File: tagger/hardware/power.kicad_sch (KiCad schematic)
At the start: 14 parts, among them J6 TETHER_POWER, U15 TPS560200

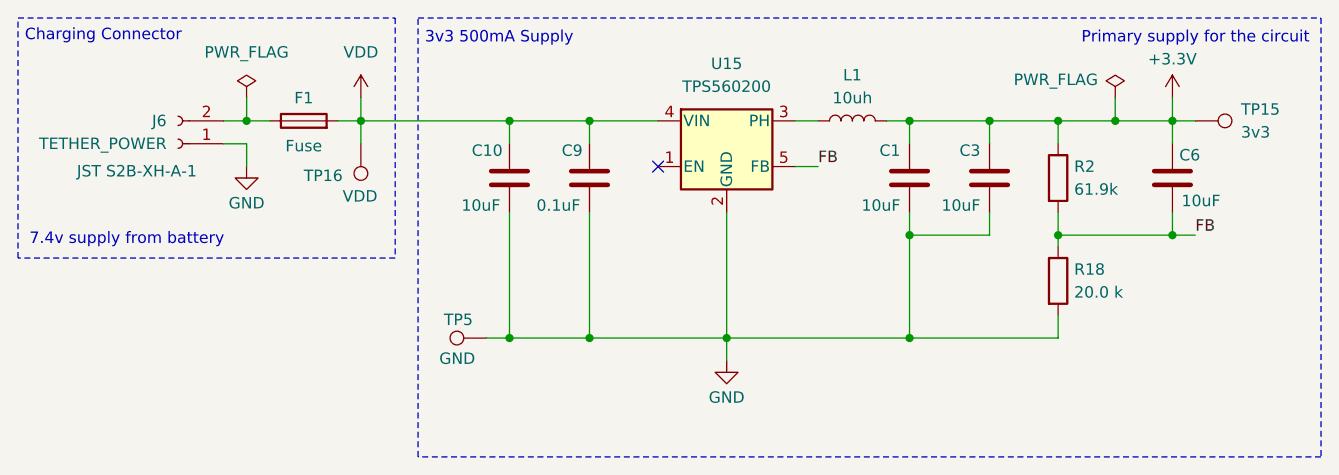
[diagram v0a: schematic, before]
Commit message: feat: schematic organization, added SD card connections
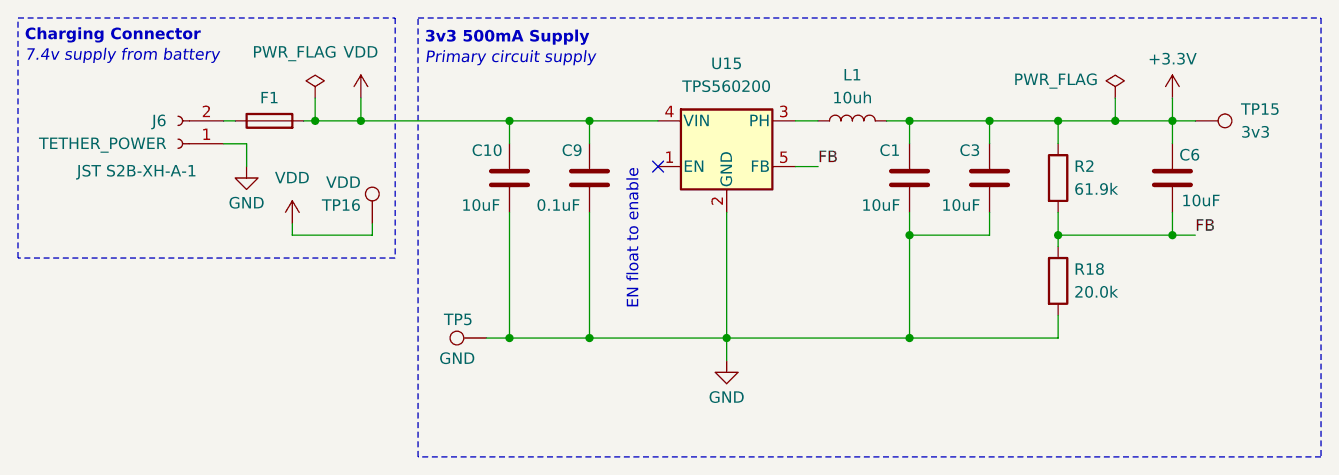
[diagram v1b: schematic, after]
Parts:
- R18: value 20.0 k -> 20.0k
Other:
- note added: "EN float to enable"
- note added: "Primary circuit supply"
- note removed: "Primary supply for the circuit"
- moved on the sheet: F1, TP16
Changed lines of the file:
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@@
 			(font
 				(size 1.27 1.27)
+				(thickness 0.254)
+				(bold yes)
 			)
 			(justify left top)
@@
 	(text "7.4v supply from battery"
 		(exclude_from_sim no)
-		(at 19.05 43.18 0)
+		(at 18.542 21.336 0)
+		(effects
+			(font
+				(size 1.27 1.27)
+				(italic yes)
+				(color 194 194 194 1)
+			)
+			(justify left top)
+		)
+	)
+	(text "Primary circuit supply"
+		(exclude_from_sim no)
+		(at 62.992 21.59 0)
+		(effects
+			(font
+				(size 1.27 1.27)
+				(italic yes)
+				(color 194 194 194 1)
+			)
+			(justify left top)
+		)
+	)
+	(text "EN float to enable"
+		(exclude_from_sim no)
+		(at 86.106 42.418 90)
 		(effects
 			(font
@@
 				(color 132 132 132 1)
 			)
-			(justify left bottom)
-		)
-	)
-	(text "Primary supply for the circuit"
-		(exclude_from_sim no)
-		(at 161.29 19.304 0)
-		(effects
-			(font
-				(size 1.27 1.27)
-				(color 132 132 132 1)
-			)
-			(justify right top)
 		)
 	)
@@
 			(font
 				(size 1.27 1.27)
+				(thickness 0.254)
+				(bold yes)
 			)
 			(justify left top)
@@
 	)
 	(junction
-		(at 133.35 41.91)
+		(at 50.8 29.21)
 		(diameter 0)
 		(color 0 0 0 0)
 	)
 	(junction
-		(at 43.18 29.21)
+		(at 133.35 41.91)
 		(diameter 0)
 		(color 0 0 0 0)
@@
 	(wire
 		(pts
-			(xy 55.88 29.21) (xy 55.88 31.75)
+			(xy 57.15 40.64) (xy 57.15 41.91)
 		)
 		(stroke
@@
 	(wire
 		(pts
-			(xy 53.34 29.21) (xy 55.88 29.21)
-		)
-		(stroke
-			(width 0)
-			(type default)
-		)
-	)
-	(wire
-		(pts
 			(xy 72.39 39.37) (xy 72.39 53.34)
 		)
@@
 	(wire
 		(pts
+			(xy 48.26 41.91) (xy 57.15 41.91)
+		)
+		(stroke
+			(width 0)
+			(type default)
+		)
+	)
+	(wire
+		(pts
 			(xy 133.35 50.8) (xy 133.35 53.34)
 		)
@@
 	(wire
 		(pts
+			(xy 48.26 40.64) (xy 48.26 41.91)
+		)
+		(stroke
+			(width 0)
+			(type default)
+		)
+	)
+	(wire
+		(pts
 			(xy 125.73 29.21) (xy 125.73 31.75)
 		)
@@
 	(wire
 		(pts
-			(xy 43.18 26.67) (xy 43.18 29.21)
+			(xy 50.8 26.67) (xy 50.8 29.21)
 		)
 		(stroke
@@
 	(wire
 		(pts
-			(xy 40.64 29.21) (xy 43.18 29.21)
+			(xy 40.64 29.21) (xy 41.91 29.21)
 		)
 		(stroke
@@
 	(wire
 		(pts
+			(xy 50.8 29.21) (xy 55.88 29.21)
+		)
+		(stroke
+			(width 0)
+			(type default)
+		)
+	)
+	(wire
+		(pts
 			(xy 146.05 29.21) (xy 148.59 29.21)
 		)
@@
 	(wire
 		(pts
-			(xy 43.18 29.21) (xy 45.72 29.21)
-		)
-		(stroke
-			(width 0)
-			(type default)
-		)
-	)
-	(wire
-		(pts
 			(xy 116.84 41.91) (xy 116.84 53.34)
 		)
@@
 		(pts
 			(xy 116.84 29.21) (xy 125.73 29.21)
+		)
+		(stroke
+			(width 0)
+			(type default)
+		)
+	)
+	(wire
+		(pts
+			(xy 49.53 29.21) (xy 50.8 29.21)
 		)
 		(stroke
@@
 	(symbol
 		(lib_id "power:PWR_FLAG")
-		(at 43.18 26.67 0)
+		(at 50.8 26.67 0)
 		(unit 1)
 		(exclude_from_sim no)
@@
 		(on_board yes)
 		(dnp no)
-		(fields_autoplaced yes)
 		(property "Reference" "#FLG01"
-			(at 43.18 24.765 0)
+			(at 50.8 24.765 0)
 			(effects
 				(font
@@
 		)
 		(property "Value" "PWR_FLAG"
-			(at 43.18 21.59 0)
+			(at 48.514 21.59 0)
 			(effects
 				(font
@@
 		)
 		(property "Footprint" ""
-			(at 43.18 26.67 0)
+			(at 50.8 26.67 0)
 			(effects
 				(font
@@
 		)
 		(property "Datasheet" "~"
-			(at 43.18 26.67 0)
+			(at 50.8 26.67 0)
 			(effects
 				(font
@@
 		)
 		(property "Description" "Special symbol for telling ERC where power comes from"
-			(at 43.18 26.67 0)
+			(at 50.8 26.67 0)
 			(effects
 				(font
@@
 	(symbol
 		(lib_id "Connector:TestPoint")
-		(at 55.88 31.75 0)
-		(mirror x)
+		(at 57.15 40.64 0)
 		(unit 1)
 		(exclude_from_sim no)
@@
 		(dnp no)
 		(property "Reference" "TP16"
-			(at 49.53 35.306 0)
-			(effects
-				(font
-					(size 1.27 1.27)
-				)
-				(justify left)
+			(at 55.88 38.608 0)
+			(effects
+				(font
+					(size 1.27 1.27)
+				)
+				(justify right)
 			)
 		)
 		(property "Value" "VDD"
-			(at 53.848 37.592 0)
-			(effects
-				(font
-					(size 1.27 1.27)
-				)
-				(justify left)
+			(at 55.88 36.068 0)
+			(effects
+				(font
+					(size 1.27 1.27)
+				)
+				(justify right)
 			)
 		)
 		(property "Footprint" "TestPoint:TestPoint_Pad_D1.5mm"
-			(at 60.96 31.75 0)
+			(at 62.23 40.64 0)
 			(effects
 				(font
@@
 		)
 		(property "Datasheet" "~"
-			(at 60.96 31.75 0)
+			(at 62.23 40.64 0)
 			(effects
 				(font
@@
 		)
 		(property "Description" "test point"
-			(at 55.88 31.75 0)
+			(at 57.15 40.64 0)
 			(effects
 				(font
@@
 		)
 		(property "Height" ""
-			(at 55.88 31.75 0)
+			(at 57.15 40.64 0)
 			(effects
 				(font
@@
 		)
 		(property "Manufacturer_Name" ""
-			(at 55.88 31.75 0)
+			(at 57.15 40.64 0)
 			(effects
 				(font
@@
 		)
 		(property "Manufacturer_Part_Number" ""
-			(at 55.88 31.75 0)
+			(at 57.15 40.64 0)
 			(effects
 				(font
@@
 		)
 		(property "Mouser Part Number" ""
-			(at 55.88 31.75 0)
+			(at 57.15 40.64 0)
 			(effects
 				(font
@@
 		)
 		(property "Mouser Price/Stock" ""
-			(at 55.88 31.75 0)
+			(at 57.15 40.64 0)
 			(effects
 				(font
@@
 		)
 		(property "JLC" ""
-			(at 55.88 31.75 0)
+			(at 57.15 40.64 0)
 			(effects
 				(font
@@
 	(symbol
 		(lib_id "Device:Fuse")
-		(at 49.53 29.21 90)
+		(at 45.72 29.21 90)
 		(unit 1)
 		(exclude_from_sim no)
@@
 		(dnp no)
 		(property "Reference" "F1"
-			(at 49.53 26.67 90)
+			(at 45.72 26.67 90)
 			(effects
 				(font
@@
 		)
 		(property "Value" "Fuse"
-			(at 49.53 32.004 90)
-			(effects
-				(font
-					(size 1.27 1.27)
-				)
+			(at 45.72 31.496 90)
+			(effects
+				(font
+					(size 1.27 1.27)
+				)
+				(hide yes)
 			)
 		)
 		(property "Footprint" "Fuse:Fuse_0805_2012Metric"
-			(at 49.53 30.988 90)
+			(at 45.72 30.988 90)
 			(effects
 				(font
@@
 		)
 		(property "Datasheet" "~"
-			(at 49.53 29.21 0)
+			(at 45.72 29.21 0)
 			(effects
 				(font
@@
 		)
 		(property "Description" "Fuse"
-			(at 49.53 29.21 0)
+			(at 45.72 29.21 0)
 			(effects
 				(font
@@
 		)
 		(property "JLC" ""
-			(at 49.53 29.21 0)
+			(at 45.72 29.21 0)
 			(effects
 				(font
@@
 	)
 	(symbol
+		(lib_id "power:VDD")
+		(at 48.26 40.64 0)
+		(unit 1)
+		(exclude_from_sim no)
+		(in_bom yes)
+		(on_board yes)
+		(dnp no)
+		(fields_autoplaced yes)
+		(property "Reference" "#PWR04"
+			(at 48.26 44.45 0)
+			(effects
+				(font
+					(size 1.27 1.27)
+				)
+				(hide yes)
+			)
+		)
+		(property "Value" "VDD"
+			(at 48.26 35.56 0)
+			(effects
+				(font
+					(size 1.27 1.27)
+				)
+			)
+		)
+		(property "Footprint" ""
+			(at 48.26 40.64 0)
+			(effects
+				(font
+					(size 1.27 1.27)
+				)
+				(hide yes)
+			)
+		)
+		(property "Datasheet" ""
+			(at 48.26 40.64 0)
+			(effects
+				(font
+					(size 1.27 1.27)
+				)
+				(hide yes)
+			)
+		)
+		(property "Description" "Power symbol creates a global label with name \"VDD\""
+			(at 48.26 40.64 0)
+			(effects
+				(font
+					(size 1.27 1.27)
+				)
+				(hide yes)
+			)
+		)
+		(pin "1"
+		)
+		(instances
+			(project "tagger"
+				(path "/7f9981c1-8446-4881-979b-6d88a629918c/71e7c18f-1f33-427d-8bd6-9eec09af0cc4"
+					(reference "#PWR04")
+					(unit 1)
+				)
+			)
+		)
+	)
+	(symbol
 		(lib_id "Device:R")
 		(at 133.35 46.99 0)
@@
 			)
 		)
-		(property "Value" "20.0 k"
+		(property "Value" "20.0k"
 			(at 135.128 48.26 0)
 			(effects

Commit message: feat: replace RS485 transceiver, fix DRC warnings
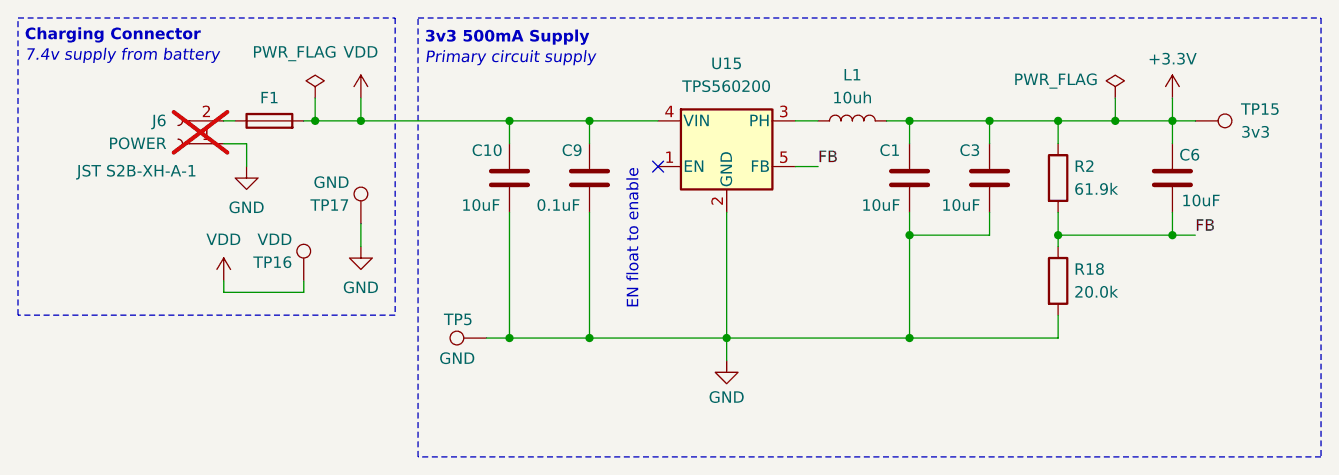
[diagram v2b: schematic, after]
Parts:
- added TP17: GND, TestPoint:TestPoint_Pad_D1.5mm, symbol Connector:TestPoint
- J6: value TETHER_POWER -> POWER; now not fitted
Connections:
- net GND: now also TP17.1
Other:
- moved on the sheet: TP16
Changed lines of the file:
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@@
 	(rectangle
 		(start 17.78 17.78)
-		(end 59.69 44.45)
+		(end 59.69 50.8)
 		(stroke
 			(width 0)
@@
 	(wire
 		(pts
-			(xy 57.15 40.64) (xy 57.15 41.91)
+			(xy 49.53 46.99) (xy 49.53 48.26)
 		)
 		(stroke
@@
 	(wire
 		(pts
-			(xy 48.26 41.91) (xy 57.15 41.91)
+			(xy 40.64 48.26) (xy 49.53 48.26)
 		)
 		(stroke
@@
 	(wire
 		(pts
-			(xy 48.26 40.64) (xy 48.26 41.91)
+			(xy 55.88 40.64) (xy 55.88 43.18)
+		)
+		(stroke
+			(width 0)
+			(type default)
+		)
+	)
+	(wire
+		(pts
+			(xy 40.64 46.99) (xy 40.64 48.26)
 		)
 		(stroke
@@
 				(path "/7f9981c1-8446-4881-979b-6d88a629918c/71e7c18f-1f33-427d-8bd6-9eec09af0cc4"
 					(reference "#PWR018")
+					(unit 1)
+				)
+			)
+		)
+	)
+	(symbol
+		(lib_id "power:GND")
+		(at 55.88 43.18 0)
+		(unit 1)
+		(exclude_from_sim no)
+		(in_bom yes)
+		(on_board yes)
+		(dnp no)
+		(property "Reference" "#PWR021"
+			(at 55.88 49.53 0)
+			(effects
+				(font
+					(size 1.27 1.27)
+				)
+				(hide yes)
+			)
+		)
+		(property "Value" "GND"
+			(at 55.88 47.752 0)
+			(effects
+				(font
+					(size 1.27 1.27)
+				)
+			)
+		)
+		(property "Footprint" ""
+			(at 55.88 43.18 0)
+			(effects
+				(font
+					(size 1.27 1.27)
+				)
+				(hide yes)
+			)
+		)
+		(property "Datasheet" ""
+			(at 55.88 43.18 0)
+			(effects
+				(font
+					(size 1.27 1.27)
+				)
+				(hide yes)
+			)
+		)
+		(property "Description" "Power symbol creates a global label with name \"GND\" , ground"
+			(at 55.88 43.18 0)
+			(effects
+				(font
+					(size 1.27 1.27)
+				)
+				(hide yes)
+			)
+		)
+		(pin "1"
+		)
+		(instances
+			(project "tagger"
+				(path "/7f9981c1-8446-4881-979b-6d88a629918c/71e7c18f-1f33-427d-8bd6-9eec09af0cc4"
+					(reference "#PWR021")
+					(unit 1)
+				)
+			)
+		)
+	)
+	(symbol
+		(lib_id "Connector:TestPoint")
+		(at 55.88 40.64 0)
+		(unit 1)
+		(exclude_from_sim no)
+		(in_bom yes)
+		(on_board yes)
+		(dnp no)
+		(property "Reference" "TP17"
+			(at 54.61 38.608 0)
+			(effects
+				(font
+					(size 1.27 1.27)
+				)
+				(justify right)
+			)
+		)
+		(property "Value" "GND"
+			(at 54.61 36.068 0)
+			(effects
+				(font
+					(size 1.27 1.27)
+				)
+				(justify right)
+			)
+		)
+		(property "Footprint" "TestPoint:TestPoint_Pad_D1.5mm"
+			(at 60.96 40.64 0)
+			(effects
+				(font
+					(size 1.27 1.27)
+				)
+				(hide yes)
+			)
+		)
+		(property "Datasheet" "~"
+			(at 60.96 40.64 0)
+			(effects
+				(font
+					(size 1.27 1.27)
+				)
+				(hide yes)
+			)
+		)
+		(property "Description" "test point"
+			(at 55.88 40.64 0)
+			(effects
+				(font
+					(size 1.27 1.27)
+				)
+				(hide yes)
+			)
+		)
+		(property "Height" ""
+			(at 55.88 40.64 0)
+			(effects
+				(font
+					(size 1.27 1.27)
+				)
+			)
+		)
+		(property "Manufacturer_Name" ""
+			(at 55.88 40.64 0)
+			(effects
+				(font
+					(size 1.27 1.27)
+				)
+			)
+		)
+		(property "Manufacturer_Part_Number" ""
+			(at 55.88 40.64 0)
+			(effects
+				(font
+					(size 1.27 1.27)
+				)
+			)
+		)
+		(property "Mouser Part Number" ""
+			(at 55.88 40.64 0)
+			(effects
+				(font
+					(size 1.27 1.27)
+				)
+			)
+		)
+		(property "Mouser Price/Stock" ""
+			(at 55.88 40.64 0)
+			(effects
+				(font
+					(size 1.27 1.27)
+				)
+			)
+		)
+		(property "JLC" ""
+			(at 55.88 40.64 0)
+			(effects
+				(font
+					(size 1.27 1.27)
+				)
+			)
+		)
+		(pin "1"
+		)
+		(instances
+			(project "tagger"
+				(path "/7f9981c1-8446-4881-979b-6d88a629918c/71e7c18f-1f33-427d-8bd6-9eec09af0cc4"
+					(reference "TP17")
 					(unit 1)
 				)
@@
 		(in_bom yes)
 		(on_board yes)
-		(dnp no)
+		(dnp yes)
 		(property "Reference" "J6"
 			(at 34.29 29.21 0)
@@
 			)
 		)
-		(property "Value" "TETHER_POWER"
+		(property "Value" "POWER"
 			(at 34.29 31.75 0)
 			(effects
@@
 		)
 		(property "Value" "GND"
-			(at 43.18 38.354 0)
+			(at 43.18 38.862 0)
 			(effects
 				(font
@@
 	(symbol
 		(lib_id "Connector:TestPoint")
-		(at 57.15 40.64 0)
+		(at 49.53 46.99 0)
 		(unit 1)
 		(exclude_from_sim no)
@@
 		(dnp no)
 		(property "Reference" "TP16"
-			(at 55.88 38.608 0)
+			(at 48.26 44.958 0)
 			(effects
 				(font
@@
 		)
 		(property "Value" "VDD"
-			(at 55.88 36.068 0)
+			(at 48.26 42.418 0)
 			(effects
 				(font
@@
 		)
 		(property "Footprint" "TestPoint:TestPoint_Pad_D1.5mm"
-			(at 62.23 40.64 0)
+			(at 54.61 46.99 0)
 			(effects
 				(font
@@
 		)
 		(property "Datasheet" "~"
-			(at 62.23 40.64 0)
+			(at 54.61 46.99 0)
 			(effects
 				(font
@@
 		)
 		(property "Description" "test point"
-			(at 57.15 40.64 0)
+			(at 49.53 46.99 0)
 			(effects
 				(font
@@
 		)
 		(property "Height" ""
-			(at 57.15 40.64 0)
+			(at 49.53 46.99 0)
 			(effects
 				(font
@@
 		)
 		(property "Manufacturer_Name" ""
-			(at 57.15 40.64 0)
+			(at 49.53 46.99 0)
 			(effects
 				(font
@@
 		)
 		(property "Manufacturer_Part_Number" ""
-			(at 57.15 40.64 0)
+			(at 49.53 46.99 0)
 			(effects
 				(font
@@
 		)
 		(property "Mouser Part Number" ""
-			(at 57.15 40.64 0)
+			(at 49.53 46.99 0)
 			(effects
 				(font
@@
 		)
 		(property "Mouser Price/Stock" ""
-			(at 57.15 40.64 0)
+			(at 49.53 46.99 0)
 			(effects
 				(font
@@
 		)
 		(property "JLC" ""
-			(at 57.15 40.64 0)
+			(at 49.53 46.99 0)
 			(effects
 				(font
@@
 	(symbol
 		(lib_id "power:VDD")
-		(at 48.26 40.64 0)
+		(at 40.64 46.99 0)
 		(unit 1)
 		(exclude_from_sim no)
@@
 		(on_board yes)
 		(dnp no)
-		(fields_autoplaced yes)
 		(property "Reference" "#PWR04"
-			(at 48.26 44.45 0)
+			(at 40.64 50.8 0)
 			(effects
 				(font
@@
 		)
 		(property "Value" "VDD"
-			(at 48.26 35.56 0)
+			(at 40.64 42.418 0)
 			(effects
 				(font
@@
 		)
 		(property "Footprint" ""
-			(at 48.26 40.64 0)
+			(at 40.64 46.99 0)
 			(effects
 				(font
@@
 		)
 		(property "Datasheet" ""
-			(at 48.26 40.64 0)
+			(at 40.64 46.99 0)
 			(effects
 				(font
@@
 		)
 		(property "Description" "Power symbol creates a global label with name \"VDD\""
-			(at 48.26 40.64 0)
-			(effects
-				(font
+			(at 40.64 46.99 0)
+			(effects
+				(font
